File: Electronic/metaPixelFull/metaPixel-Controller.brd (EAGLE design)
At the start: 81.3 x 64.8 mm, 17 parts, among them IC1 MAX481CPA, IC3 74HCT245N

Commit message: Layout 1
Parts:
- IC2: value TEENSY_3.1_OUTER_ROW -> TEENSY_3.1
- renumbered U$1 to IC2
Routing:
- net GND: track 0.00 -> 149.5 mm
- net VCC: track 0.00 -> 139.9 mm
- net GND_EXT: track 0.00 -> 80.2 mm
- net DMX_IN: track 0.00 -> 72.4 mm
- net +3.3V: track 0.00 -> 56.4 mm
- net !LCD_RST: track 0.00 -> 50.8 mm
- net DMX+: track 0.00 -> 46.8 mm
- net !SD_CS: track 0.00 -> 44.5 mm
- net DMX-: track 0.00 -> 41.1 mm
- net +5V_EXT: track 0.00 -> 37.4 mm
- net SCLK: track 0.00 -> 29.7 mm
- net KEY_1: track 0.00 -> 26.5 mm
- net KEY_5: track 0.00 -> 26.5 mm
- net KEY_4: track 0.00 -> 26.5 mm
- net KEY_3: track 0.00 -> 26.5 mm
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
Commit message: boards
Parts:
- SV1: value HOST -> DISPLAY
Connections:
- removed net N$14: SV1.17
- removed net N$15: SV1.15
- new net AGND: IC2.AGND
- net GND: no longer IC2.AGND
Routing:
- net !LCD_CS: track 11.2 -> 9.72 mm
- net GND: track 149.5 -> 148.4 mm
- net VCC: track 139.9 -> 139.2 mm
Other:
- board text added: "GND"
- board text added: "VCC"
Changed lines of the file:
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@@
 <layer number="45" name="Holes" color="7" fill="1" visible="yes" active="yes"/>
 <layer number="46" name="Milling" color="3" fill="1" visible="no" active="yes"/>
-<layer number="47" name="Measures" color="7" fill="1" visible="no" active="yes"/>
+<layer number="47" name="Measures" color="7" fill="1" visible="yes" active="yes"/>
 <layer number="48" name="Document" color="7" fill="1" visible="yes" active="yes"/>
 <layer number="49" name="Reference" color="7" fill="1" visible="yes" active="yes"/>
@@
 <wire x1="81.28" y1="64.77" x2="81.28" y2="0" width="0" layer="20"/>
 <wire x1="81.28" y1="0" x2="0" y2="0" width="0" layer="20"/>
+<text x="71.12" y="5.08" size="2.54" layer="25">GND</text>
+<text x="71.12" y="19.05" size="2.54" layer="25">VCC</text>
 </plain>
 <attributes>
@@
 <attribute name="MPN" value="NME1205D" x="63.5" y="16.51" size="1.778" layer="27" rot="R180" display="off"/>
 </element>
-<element name="DMX_1" library="RP025xx" package="RP025-03" value="RP025-03" x="72.39" y="35.8" rot="R270"/>
-<element name="DMX_2" library="RP025xx" package="RP025-03" value="RP025-03" x="72.39" y="50.8" rot="R270"/>
+<element name="DMX_1" library="RP025xx" package="RP025-03" value="RP025-03" x="72.39" y="35.8" smashed="yes" rot="R270">
+<attribute name="NAME" x="65.72" y="32.13" size="2.54" layer="21" rot="R270" align="bottom-center"/>
+</element>
+<element name="DMX_2" library="RP025xx" package="RP025-03" value="RP025-03" x="72.39" y="50.8" smashed="yes" rot="R270">
+<attribute name="NAME" x="65.72" y="45.86" size="2.54" layer="21" rot="R270" align="bottom-center"/>
+</element>
 <element name="IC1" library="maxim" package="DIL08" value="MAX481CPA" x="52.07" y="33.02" rot="R270">
 <attribute name="OC_NEWARK" value="99K3445" x="52.07" y="33.02" size="1.778" layer="27" rot="R270" display="off"/>
@@
 </element>
 <element name="IC3" library="74xx-eu" package="DIL20" value="74HCT245N" x="21.59" y="45.72"/>
-<element name="LED" library="RP025xx" package="RP025-02" value="RP025-02" x="15.24" y="55.88"/>
+<element name="LED" library="RP025xx" package="RP025-02" value="RP025-02" x="15.24" y="55.88" smashed="yes">
+<attribute name="NAME" x="11.75" y="57.01" size="2.54" layer="21" rot="R90" align="bottom-center"/>
+</element>
 <element name="OK1" library="optocoupler" package="DIL08" value="6N137" x="49.53" y="17.78" rot="R180">
 <attribute name="OC_NEWARK" value="52M1895" x="49.53" y="17.78" size="1.778" layer="27" rot="R180" display="off"/>
@@
 <attribute name="MPN" value="6N137" x="49.53" y="17.78" size="1.778" layer="27" rot="R180" display="off"/>
 </element>
-<element name="POWER" library="RP025xx" package="RP025-02" value="RP025-02" x="72.39" y="15.8" rot="R270"/>
+<element name="POWER" library="RP025xx" package="RP025-02" value="RP025-02" x="72.39" y="15.8" smashed="yes" rot="R270">
+<attribute name="NAME" x="65.72" y="13.4" size="2.54" layer="21" rot="R270" align="bottom-center"/>
+</element>
 <element name="R1" library="resistor" package="0207/7" value="562" x="63.5" y="45.72" rot="R270"/>
 <element name="R2" library="resistor" package="0207/7" value="562" x="63.5" y="30.48" rot="R90"/>
@@
 <element name="R4" library="rcl" package="0207/10" value="470" x="44.45" y="31.75" rot="R90"/>
 <element name="R7" library="resistor" package="0207/10" value="4k7" x="57.15" y="5.08"/>
-<element name="SV1" library="con-harting-ml" package="ML20L" value="HOST" x="30.48" y="11.43" rot="R180">
+<element name="SV1" library="con-harting-ml" package="ML20L" value="DISPLAY" x="30.48" y="11.43" smashed="yes" rot="R180">
 <attribute name="OC_NEWARK" value="unknown" x="30.48" y="11.43" size="1.778" layer="27" rot="R180" display="off"/>
 <attribute name="MF" value="" x="30.48" y="11.43" size="1.778" layer="27" rot="R180" display="off"/>
 <attribute name="OC_FARNELL" value="unknown" x="30.48" y="11.43" size="1.778" layer="27" rot="R180" display="off"/>
 <attribute name="MPN" value="" x="30.48" y="11.43" size="1.778" layer="27" rot="R180" display="off"/>
+<attribute name="NAME" x="13.9954" y="10.16" size="1.778" layer="25" ratio="10" rot="R180"/>
+<attribute name="VALUE" x="13.9954" y="6.35" size="1.778" layer="27" ratio="10" rot="R180"/>
 </element>
 <element name="IC2" library="Teensy_3_and_LC_Series_Boards_v1.0" package="TEENSY3-OUTER_ROW" value="TEENSY_3.1" x="17.78" y="27.94" rot="R90"/>
@@
 <contactref element="IC2" pad="GND"/>
 <contactref element="IC2" pad="GND1"/>
-<contactref element="IC2" pad="AGND"/>
 <contactref element="SV1" pad="1"/>
 <contactref element="OK1" pad="5"/>
@@
 <wire x1="5.08" y1="46.99" x2="3.81" y2="46.99" width="0.4064" layer="16"/>
 <wire x1="3.81" y1="46.99" x2="2.54" y2="45.72" width="0.4064" layer="16"/>
-<wire x1="2.54" y1="45.72" x2="2.54" y2="41.91" width="0.4064" layer="16"/>
-<wire x1="2.54" y1="41.91" x2="3.81" y2="40.64" width="0.4064" layer="16"/>
-<wire x1="3.81" y1="40.64" x2="3.81" y2="35.56" width="0.4064" layer="16"/>
-<wire x1="3.81" y1="35.56" x2="3.81" y2="22.86" width="0.4064" layer="16"/>
-<wire x1="3.81" y1="22.86" x2="1.27" y2="20.32" width="0.4064" layer="16"/>
+<wire x1="2.54" y1="21.59" x2="1.27" y2="20.32" width="0.4064" layer="16"/>
+<wire x1="2.54" y1="21.59" x2="2.54" y2="45.72" width="0.4064" layer="16"/>
 </signal>
 <signal name="VCC" class="1">
@@
 <wire x1="66.04" y1="15.24" x2="63.5" y2="15.24" width="0.4064" layer="1"/>
 <wire x1="53.34" y1="13.97" x2="50.8" y2="13.97" width="0.4064" layer="1"/>
-<wire x1="53.34" y1="13.97" x2="60.96" y2="13.97" width="0.4064" layer="1"/>
-<wire x1="60.96" y1="13.97" x2="60.96" y2="15.24" width="0.4064" layer="1"/>
+<wire x1="53.34" y1="13.97" x2="59.69" y2="13.97" width="0.4064" layer="1"/>
+<wire x1="59.69" y1="13.97" x2="60.96" y2="15.24" width="0.4064" layer="1"/>
 <wire x1="60.96" y1="15.24" x2="63.5" y2="15.24" width="0.4064" layer="1"/>
 <wire x1="50.8" y1="13.97" x2="50.8" y2="11.43" width="0.4064" layer="16"/>
@@
 <wire x1="39.37" y1="43.18" x2="39.37" y2="12.7" width="0.4064" layer="1"/>
 </signal>
-<signal name="LED_OUT">
+<signal name="LED_OUT" class="1">
 <contactref element="IC3" pad="18"/>
 <contactref element="LED" pad="P$1"/>
 <contactref element="LED" pad="P$2"/>
-<wire x1="15.24" y1="49.53" x2="15.24" y2="55.88" width="0.2032" layer="16"/>
-<wire x1="15.24" y1="55.88" x2="20.24" y2="55.88" width="0.2032" layer="16"/>
+<wire x1="15.24" y1="49.53" x2="15.24" y2="55.88" width="0.4064" layer="16"/>
+<wire x1="15.24" y1="55.88" x2="20.24" y2="55.88" width="0.4064" layer="16"/>
 </signal>
 <signal name="LED_OUT3V">
@@
 <contactref element="IC2" pad="10"/>
 <contactref element="SV1" pad="7"/>
-<wire x1="29.21" y1="20.32" x2="29.21" y2="19.05" width="0.2032" layer="16"/>
-<wire x1="29.21" y1="19.05" x2="30.48" y2="17.78" width="0.2032" layer="16"/>
-<wire x1="30.48" y1="17.78" x2="33.02" y2="17.78" width="0.2032" layer="16"/>
-<wire x1="33.02" y1="17.78" x2="34.29" y2="16.51" width="0.2032" layer="16"/>
-<wire x1="34.29" y1="16.51" x2="34.29" y2="12.7" width="0.2032" layer="16"/>
+<wire x1="29.21" y1="20.32" x2="34.29" y2="15.24" width="0.2032" layer="16"/>
+<wire x1="34.29" y1="15.24" x2="34.29" y2="12.7" width="0.2032" layer="16"/>
 </signal>
 <signal name="MOSI">
@@
 <wire x1="17.78" y1="11.43" x2="17.78" y2="34.29" width="0.2032" layer="1"/>
 <wire x1="17.78" y1="34.29" x2="16.51" y2="35.56" width="0.2032" layer="1"/>
-</signal>
-<signal name="N$14">
-<contactref element="SV1" pad="17"/>
-</signal>
-<signal name="N$15">
-<contactref element="SV1" pad="15"/>
 </signal>
 <signal name="DMX-" class="1">
@@
 <wire x1="50.8" y1="26.67" x2="50.8" y2="21.59" width="0.4064" layer="16"/>
 </signal>
+<signal name="AGND">
+<contactref element="IC2" pad="AGND"/>
+</signal>
 </signals>

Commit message: Fixing the boards
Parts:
- removed POWER: RP025-02, RP025xx:RP025-02
- removed SV1: DISPLAY, con-harting-ml:ML20L
- added J1: PWR, SparkFun-Connectors:POWER_JACK_SLOT
- added PWR: RP025-02, RP025xx:RP025-02
- added SK1: Display, jt-con-micromatch:AMP-215079-20
- moved R7 10.2 mm to (57.1, 15.2)
- moved DMX_1 8.89 mm to (72.4, 44.7)
- moved DMX_2 8.89 mm to (72.4, 59.7)
- moved DC1 7.73 mm to (62.2, 24.1)
- moved OK1 7.62 mm to (49.5, 25.4)
- moved C1 6.35 mm to (52.1, 48.3)
- moved R1 6.35 mm to (63.5, 52.1)
- moved R3 6.35 mm to (61.0, 44.5)
- moved R4 6.35 mm to (44.5, 38.1)
- moved R2 6.35 mm to (63.5, 36.8)
- moved IC1 6.35 mm to (52.1, 39.4)
- moved LED 2.54 mm to (15.2, 58.4)
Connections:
- removed net !SD_CS: IC2.21/A7, SV1.11
- removed net ENC_DIR: IC2.20/A6, SV1.20
- removed net ENC_STEP: IC2.19/A5, SV1.19
- new net !MEM_CS: IC2.21/A7, SK1.13
- new net ENC_A: IC2.14/A0, SK1.14
- new net ENC_B: IC2.15/A1, SK1.15
- net !LCD_CS: now also SK1.6; no longer SV1.7
- net !LCD_RST: now also SK1.7; no longer SV1.2
- net +3.3V: now also SK1.17, SK1.19; no longer SV1.13
- net GND: now also J1.GND@1, PWR.P$2, SK1.16, SK1.18, SK1.20; no longer POWER.P$2, SV1.1
- net KEY_1: now also IC2.20/A6, SK1.1; no longer IC2.14/A0, SV1.10
- net KEY_2: now also IC2.19/A5, SK1.2; no longer IC2.15/A1, SV1.12
- net KEY_3: now also IC2.18/A4, SK1.3; no longer IC2.16/A2, SV1.14
- net KEY_4: now also SK1.4; no longer SV1.16
- net KEY_5: now also IC2.16/A2, SK1.5; no longer IC2.18/A4, SV1.18
- net LCD_DC: now also SK1.8; no longer SV1.8
- net LCD_LED: now also SK1.11; no longer SV1.5
- net LED_OUT: no longer LED.P$2
- net MISO: now also SK1.12; no longer SV1.9
- net MOSI: now also SK1.9; no longer SV1.4
- net SCLK: now also SK1.10; no longer SV1.6
- net VCC: now also J1.PWR, PWR.P$1; no longer POWER.P$1, SV1.3
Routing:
- net !SD_CS: track 44.5 -> 0.00 mm
- net !MEM_CS: track 0.00 -> 42.0 mm
- net ENC_B: track 0.00 -> 27.7 mm
- net !LCD_RST: track 50.8 -> 23.4 mm
- net ENC_DIR: track 26.5 -> 0.00 mm
- net ENC_STEP: track 23.9 -> 0.00 mm
- net ENC_A: track 0.00 -> 23.9 mm
- net GND: track 148.4 -> 169.2 mm, vias 0 -> 1
- net VCC: track 139.2 -> 126.1 mm
- net +3.3V: track 56.4 -> 69.1 mm
- net MISO: track 21.4 -> 10.8 mm
- net !LCD_CS: track 9.72 -> 17.3 mm
- net DMX_IN: track 72.4 -> 80.0 mm
- net LCD_LED: track 22.9 -> 28.4 mm, vias 0 -> 1
- net MOSI: track 18.1 -> 13.9 mm
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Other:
- board size 81.3 x 64.8 mm -> 81.3 x 67.3 mm

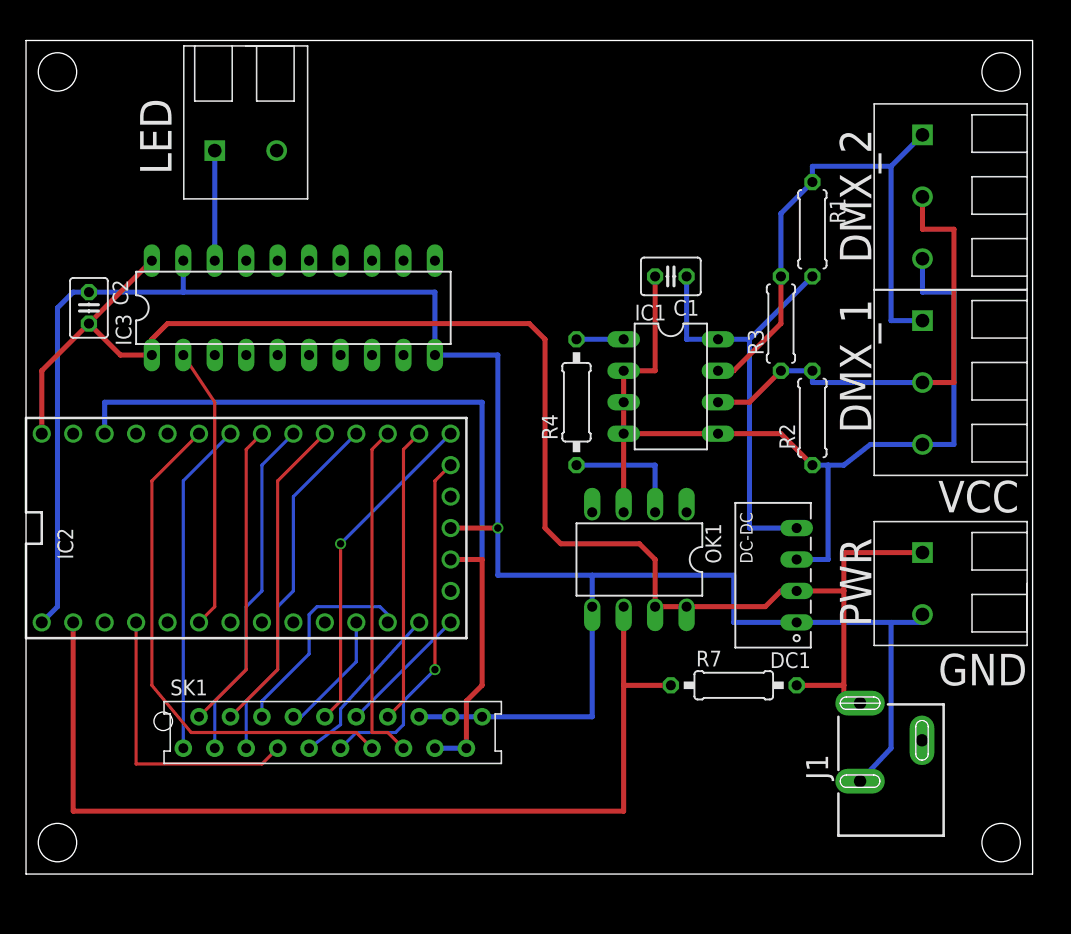
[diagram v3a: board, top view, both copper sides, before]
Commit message: fixing size issue
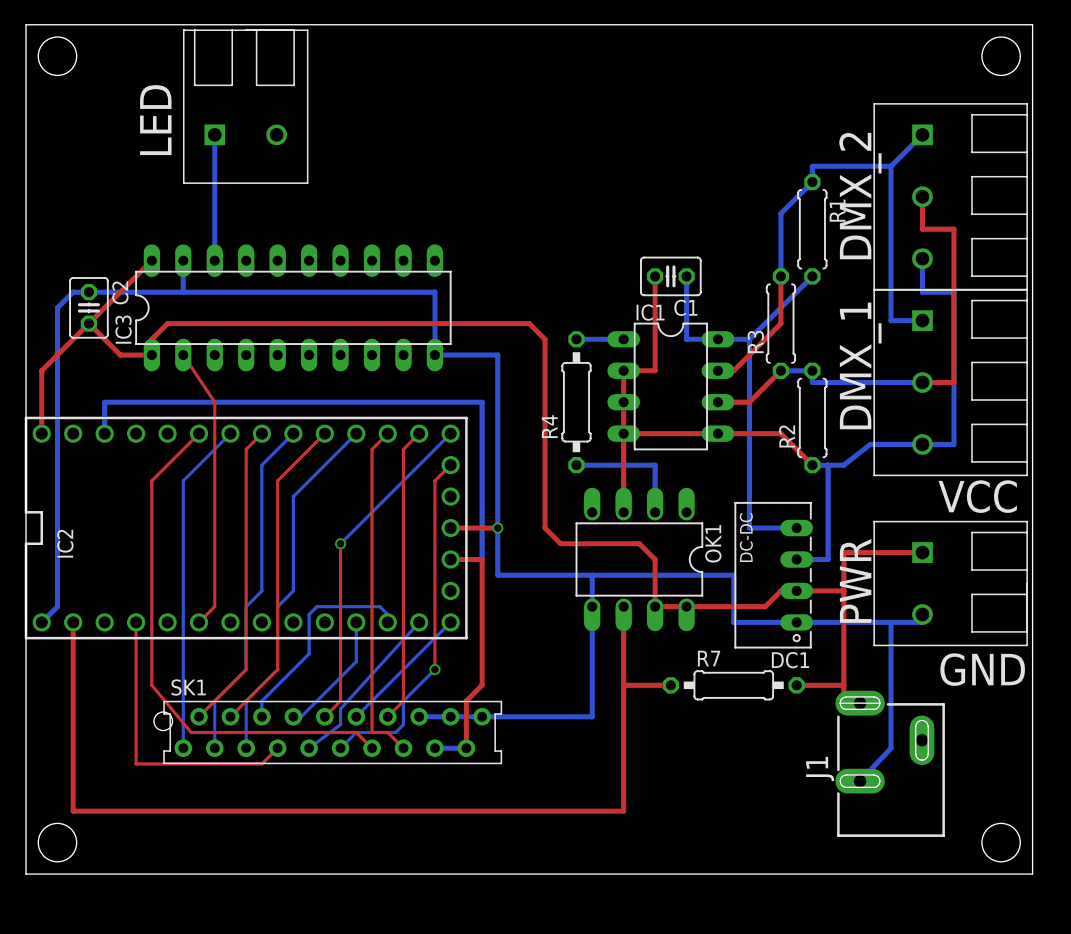
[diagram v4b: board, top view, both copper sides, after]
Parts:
- moved LED 1.27 mm to (15.2, 59.7)
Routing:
- net LED_OUT: track 8.89 -> 10.2 mm
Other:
- board size 81.3 x 67.3 mm -> 81.3 x 68.6 mm
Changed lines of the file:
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@@
 <board>
 <plain>
-<hole x="2.54" y="64.77" drill="3.1"/>
+<hole x="2.54" y="66.04" drill="3.1"/>
 <hole x="2.54" y="2.54" drill="3.1"/>
-<hole x="78.74" y="64.77" drill="3.1"/>
+<hole x="78.74" y="66.04" drill="3.1"/>
 <hole x="78.74" y="2.54" drill="3.1"/>
-<wire x1="0" y1="0" x2="0" y2="67.31" width="0" layer="20"/>
-<wire x1="0" y1="67.31" x2="81.28" y2="67.31" width="0" layer="20"/>
-<wire x1="81.28" y1="67.31" x2="81.28" y2="0" width="0" layer="20"/>
+<wire x1="0" y1="0" x2="0" y2="68.58" width="0" layer="20"/>
+<wire x1="0" y1="68.58" x2="81.28" y2="68.58" width="0" layer="20"/>
+<wire x1="81.28" y1="68.58" x2="81.28" y2="0" width="0" layer="20"/>
 <wire x1="81.28" y1="0" x2="0" y2="0" width="0" layer="20"/>
 <text x="73.66" y="15.24" size="2.54" layer="25">GND</text>
@@
 </element>
 <element name="IC3" library="74xx-eu" package="DIL20" value="74HCT245N" x="21.59" y="45.72"/>
-<element name="LED" library="RP025xx" package="RP025-02" value="RP025-02" x="15.24" y="58.42" smashed="yes">
-<attribute name="NAME" x="11.75" y="59.55" size="2.54" layer="21" rot="R90" align="bottom-center"/>
+<element name="LED" library="RP025xx" package="RP025-02" value="RP025-02" x="15.24" y="59.69" smashed="yes">
+<attribute name="NAME" x="11.75" y="60.82" size="2.54" layer="21" rot="R90" align="bottom-center"/>
 </element>
 <element name="OK1" library="optocoupler" package="DIL08" value="6N137" x="49.53" y="25.4" rot="R180">
@@
 <contactref element="IC3" pad="18"/>
 <contactref element="LED" pad="P$1"/>
-<wire x1="15.24" y1="49.53" x2="15.24" y2="58.42" width="0.4064" layer="16"/>
+<wire x1="15.24" y1="49.53" x2="15.24" y2="59.69" width="0.4064" layer="16"/>
 </signal>
 <signal name="LED_OUT3V">

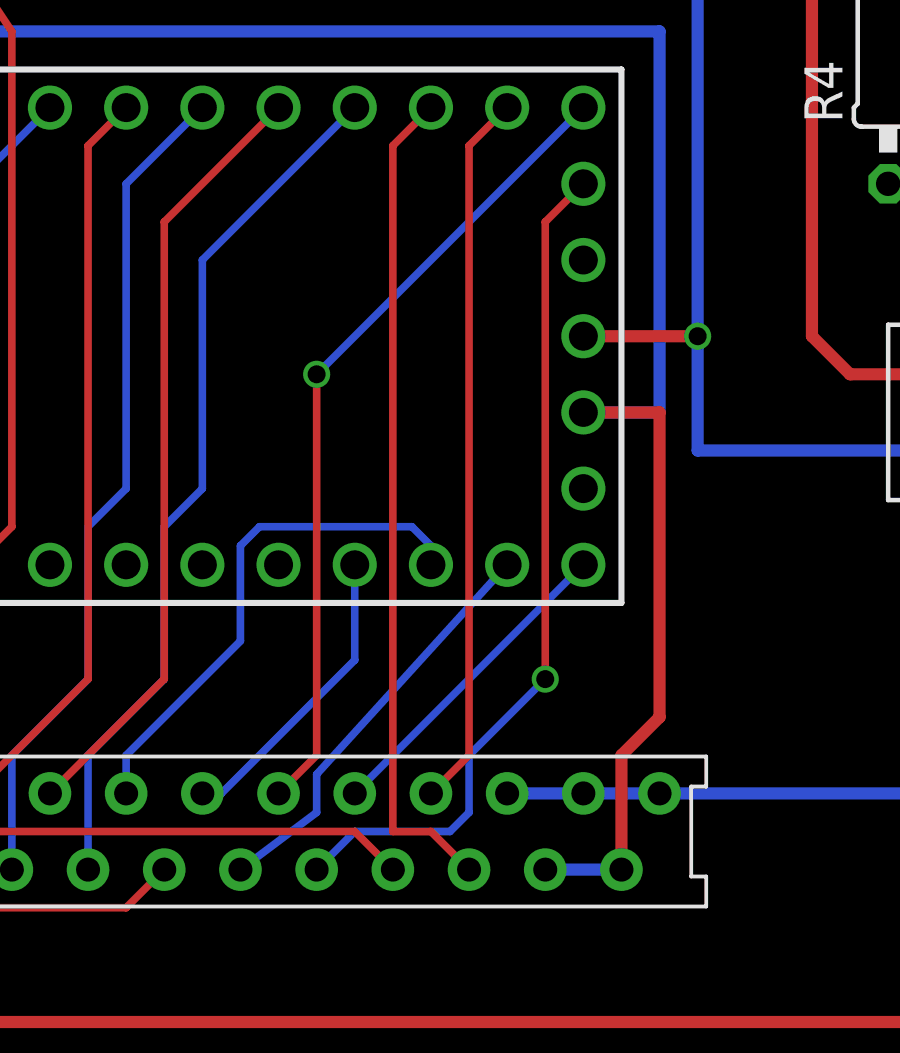
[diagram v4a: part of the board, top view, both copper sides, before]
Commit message: fixing TFT_LED problem
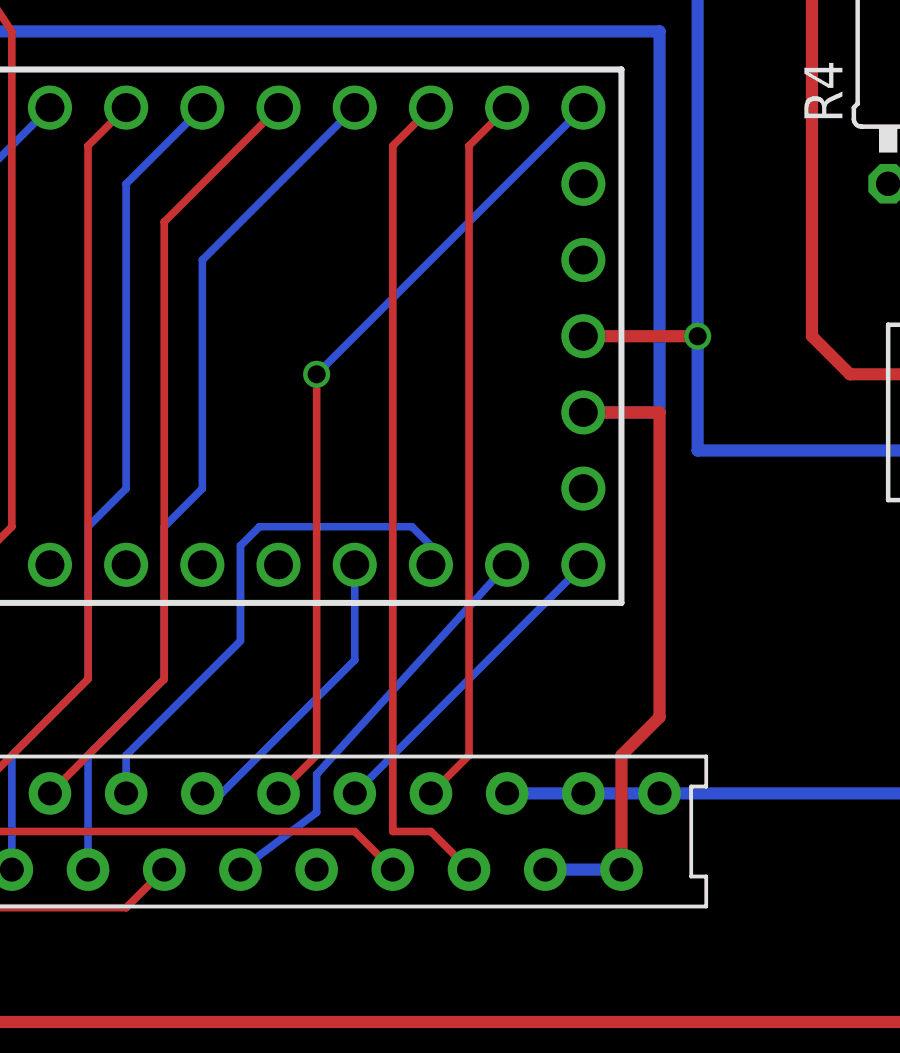
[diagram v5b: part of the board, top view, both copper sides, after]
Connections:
- net LCD_LED: now also IC2.6; no longer IC2.RESET/DAC
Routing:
- net LCD_LED: track 28.4 -> 0.00 mm, vias 1 -> 0
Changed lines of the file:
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@@
 </signal>
 <signal name="LCD_LED">
-<contactref element="IC2" pad="RESET/DAC"/>
 <contactref element="SK1" pad="11"/>
-<wire x1="25.4" y1="10.16" x2="26.67" y2="11.43" width="0.254" layer="16"/>
-<wire x1="26.67" y1="11.43" x2="29.845" y2="11.43" width="0.254" layer="16"/>
-<wire x1="29.845" y1="11.43" x2="30.48" y2="12.065" width="0.254" layer="16"/>
-<wire x1="30.48" y1="12.065" x2="30.48" y2="13.97" width="0.254" layer="16"/>
-<wire x1="30.48" y1="13.97" x2="33.02" y2="16.51" width="0.254" layer="16"/>
-<via x="33.02" y="16.51" extent="1-16" drill="0.6" shape="square"/>
-<wire x1="33.02" y1="16.51" x2="33.02" y2="31.75" width="0.254" layer="1"/>
-<wire x1="33.02" y1="31.75" x2="34.29" y2="33.02" width="0.254" layer="1"/>
+<contactref element="IC2" pad="6"/>
+<wire x1="25.4" y1="10.16" x2="19.05" y2="20.32" width="0" layer="19" extent="1-1"/>
 </signal>
 <signal name="KEY_1">
